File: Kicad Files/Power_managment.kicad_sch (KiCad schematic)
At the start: 44 parts, among them J1 HRO_Type-C-31-M-14, J2 BATTERY, Q1 2N7002, SW1 SW_Slide_DPDT, U1 SRV05-4, U10 TPS62840YBG, U2 BQ24075RGT, U3 MAX17048, U4 TPS62840YBG

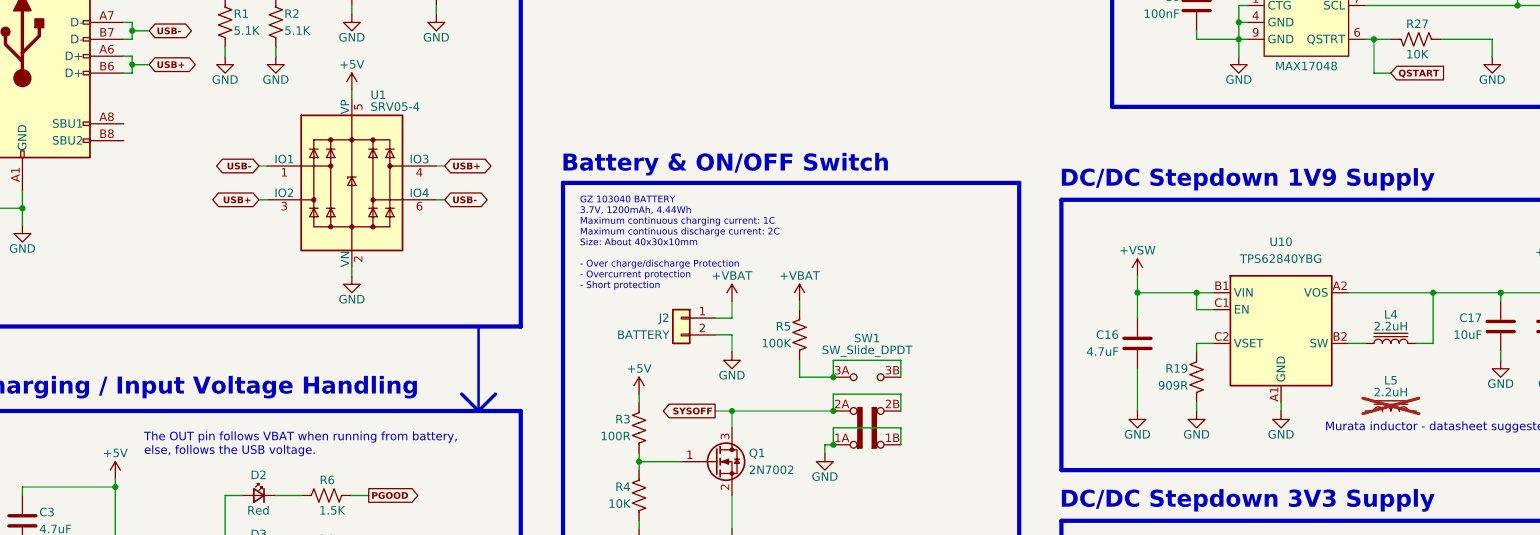
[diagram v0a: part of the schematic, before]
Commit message: Minor improvements (detailed list attached)
- Updated JST Connector to a more common PH 2.0mm one;
- Added some helpful silkscreen;
- Retouched some tracks;
- Updated schematic symbols information to help “automatically” generate JLC BOM;
- Adjusted Vias Annular ring sizes and clearances cleanup for JLC manufacturing;
- Adjusted gitgnore to include .csv and .xml to show BOM files on Github;
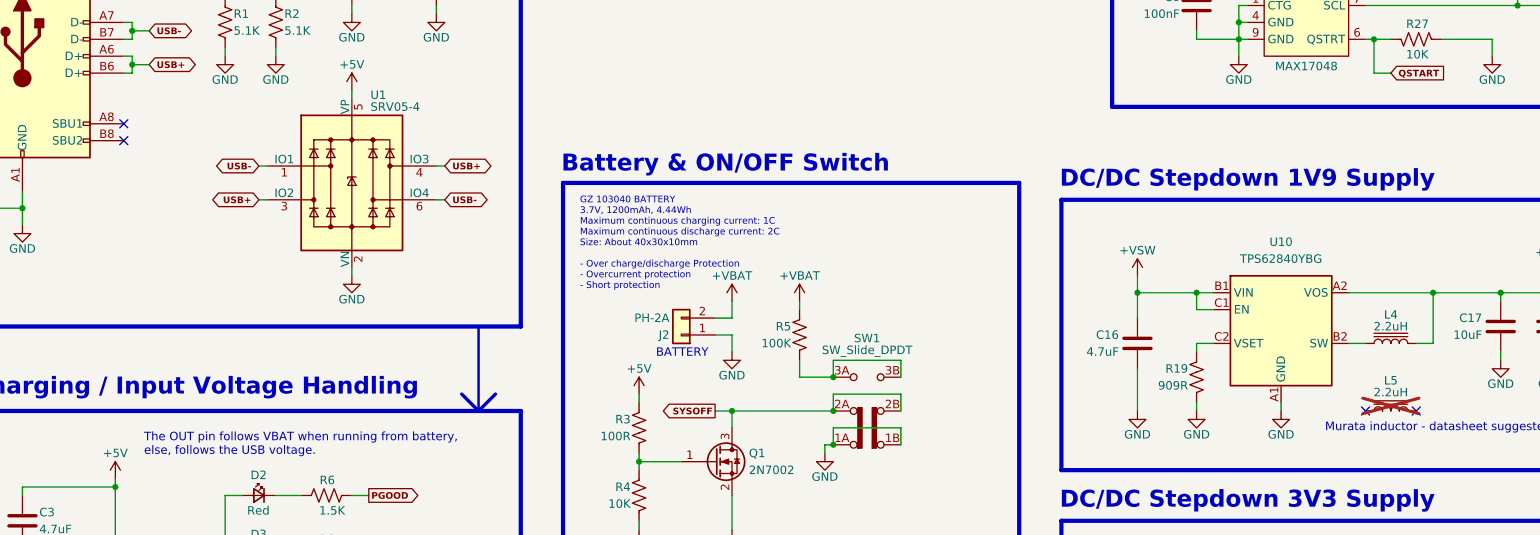
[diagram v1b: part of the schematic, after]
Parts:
- C1, C18, C9: JLC PN C95841 -> (none); JLCPCB PN (none) -> C95841
- C16, C7: JLC PN C23733 -> (none); JLCPCB PN (none) -> C23733
- C17, C8: JLC PN C15525 -> (none); JLCPCB PN (none) -> C15525
- C2: JLC PN C49678 -> (none); JLCPCB PN (none) -> C49678
- C3: JLC PN C29823 -> (none); JLCPCB PN (none) -> C29823
- C4, C5: JLC PN C6119943 -> (none); JLCPCB PN (none) -> C6119943
- C6: JLCPCB PN (none) -> C307331; Manufacturer (none) -> Samsung; Part Number (none) -> CL05B104KB54PNC
- D2: JLC PN C2286 -> (none); JLCPCB PN (none) -> C2286
- D3: JLC PN C5121471 -> (none); JLCPCB PN (none) -> C5121471
- F1: JLC PN C151139 -> (none); JLCPCB PN (none) -> C151139
- J1: JLC PN C223907 -> (none); JLCPCB PN (none) -> C223907
- J2: value BATTERY -> PH-2A; footprint Connector_JST:JST_XH_B2B-XH-AM_1x02_P2.50mm_Vertical -> Connector_JST:JST_PH_B2B-PH-K_1x02_P2.00mm_Vertical; JLCPCB PN (none) -> C2319; Manufacturer (none) -> BOOMELE(Boom Precision Elec); Part Number (none) -> PH-2A
- L1: JLC PN C88970 -> (none); JLCPCB PN (none) -> C88970
- L3, L4: JLC PN C5832372 -> (none); JLCPCB PN (none) -> C5832372
- L5: JLC PN C337893 -> (none); JLCPCB PN (none) -> C337893
- Q1: JLC PN C8545 -> (none); JLCPCB PN (none) -> C8545
- R1, R2: JLCPCB PN (none) -> C23186; Manufacturer (none) -> UNI-ROYAL(Uniroyal Elec); Part Number (none) -> 0603WAF5101T5E
- R10, R9: JLCPCB PN (none) -> C25804; Manufacturer (none) -> UNI-ROYAL(Uniroyal Elec); Part Number (none) -> 0603WAF1002T5E; now left out of the parts list
- R11: JLC PN C2998050 -> (none); JLCPCB PN (none) -> C2998050
- R12: JLCPCB PN (none) -> C23018; Manufacturer (none) -> UNI-ROYAL(Uniroyal Elec); Part Number (none) -> 0603WAF3901T5E
- R13: JLCPCB PN (none) -> C25879; Manufacturer (none) -> UNI-ROYAL(Uniroyal Elec); Part Number (none) -> 0402WGF2201TCE
- R14: JLCPCB PN (none) -> C25796; Manufacturer (none) -> UNI-ROYAL(Uniroyal Elec); Part Number (none) -> 0402WGF5602TCE
- R19: JLC PN C471842 -> (none); JLCPCB PN (none) -> C471842
- R27, R4: JLCPCB PN (none) -> C25804; Manufacturer (none) -> UNI-ROYAL(Uniroyal Elec); Part Number (none) -> 0603WAF1002T5E
- R3: JLCPCB PN (none) -> C22775; Manufacturer (none) -> UNI-ROYAL(Uniroyal Elec); Part Number (none) -> 0603WAF1000T5E
- R5: JLCPCB PN (none) -> C25803; Manufacturer (none) -> UNI-ROYAL(Uniroyal Elec); Part Number (none) -> 0603WAF1003T5E
- R6, R8: JLCPCB PN (none) -> C22843; Manufacturer (none) -> UNI-ROYAL(Uniroyal Elec); Part Number (none) -> 0603WAF1501T5E
- R7: JLCPCB PN (none) -> C17414; Manufacturer (none) -> UNI-ROYAL(Uniroyal Elec); Part Number (none) -> 0805W8F1002T5E
- SW1: now left out of the parts list
- U1: JLC PN C2836319 -> (none); JLCPCB PN (none) -> C2836319
- U10, U4: JLCPCB PN (none) -> C2071139; Manufacturer (none) -> Texas Instruments; Part Number (none) -> TPS62840YBGR
- U2: JLCPCB PN (none) -> C15464; Manufacturer (none) -> Texas Instruments; Part Number (none) -> BQ24075RGTR
- U3: JLCPCB PN (none) -> C2682616; Part Number (none) -> MAX17048G+T10
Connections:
- net +VBAT: now also J2.2 (Pin_2); no longer J2.1 (Pin_1)
- net GND: now also J2.1 (Pin_1); no longer J2.2 (Pin_2)
- no-connect marks 1 -> 5
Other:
- note added: "BATTERY"
- moved on the sheet: J2
